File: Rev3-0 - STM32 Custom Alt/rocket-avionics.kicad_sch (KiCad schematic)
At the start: 0 parts

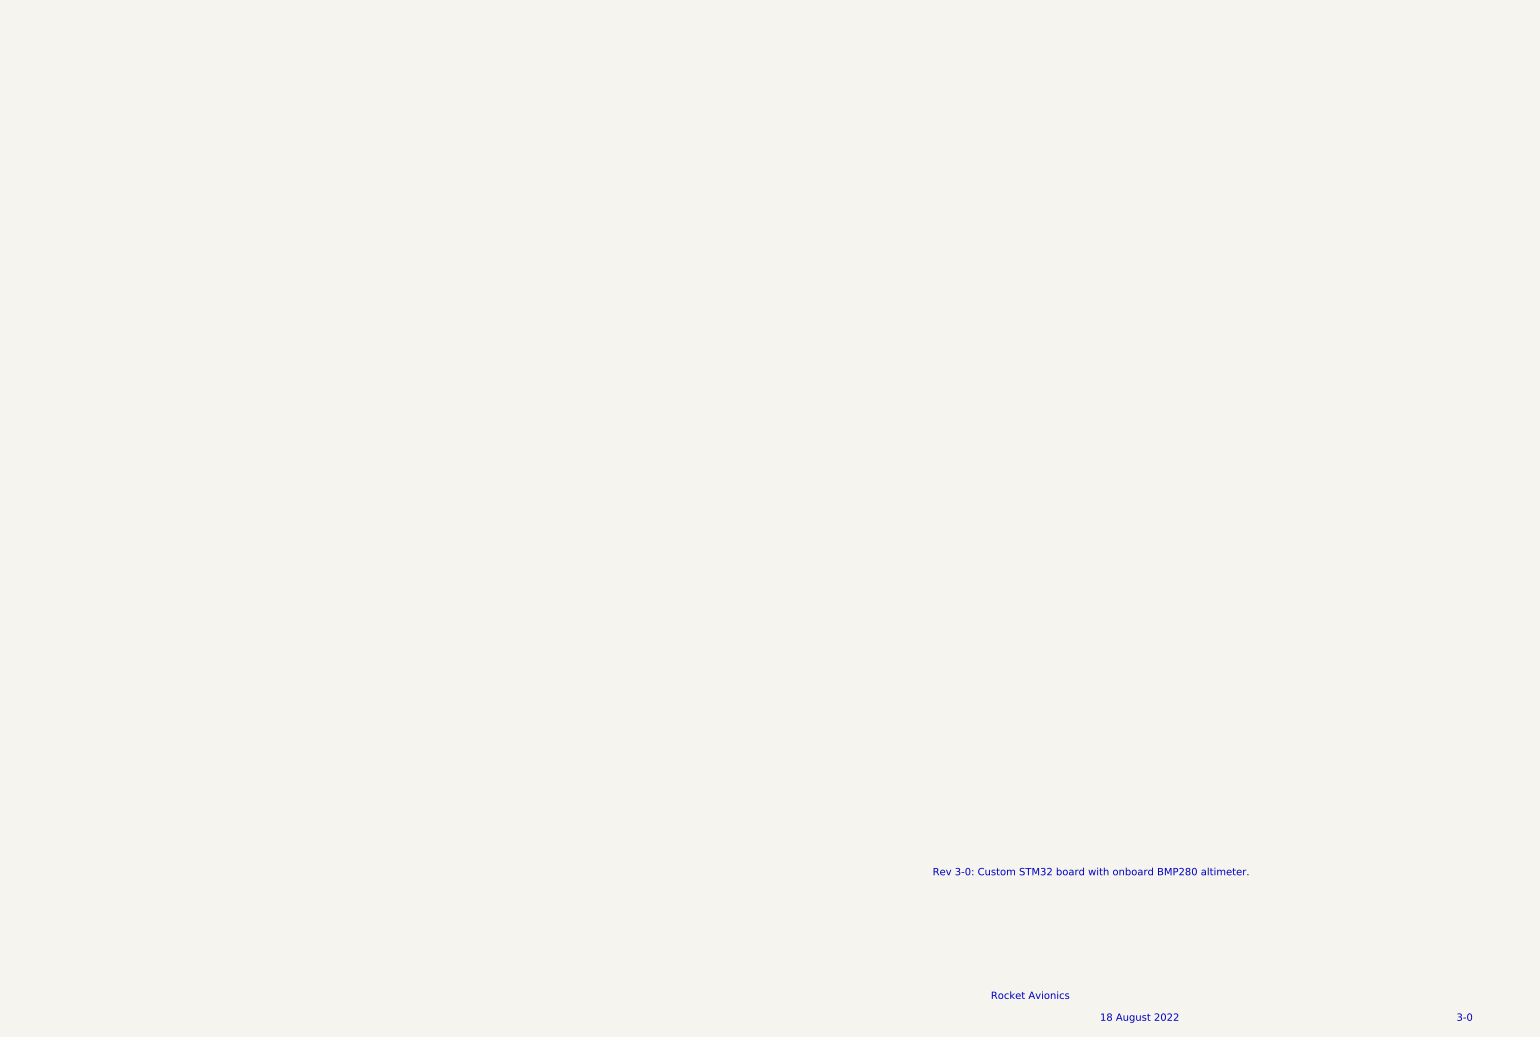
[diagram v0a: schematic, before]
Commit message: Draft schematic for core STM32 circuit.
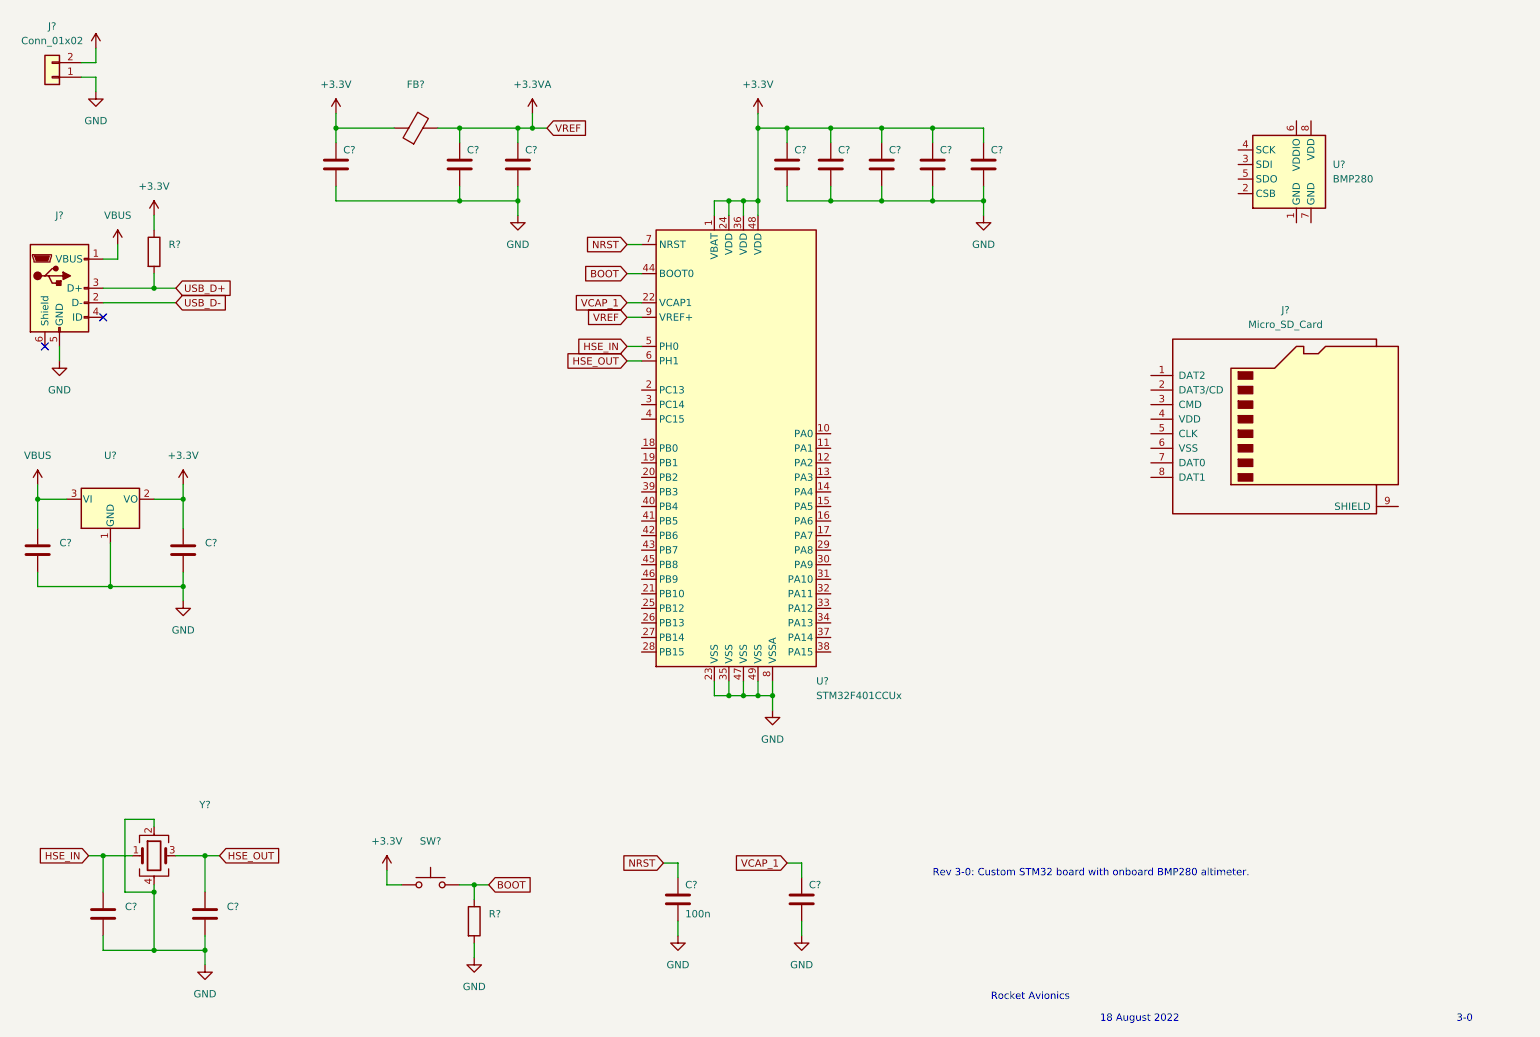
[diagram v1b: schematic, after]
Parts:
- added C? (x13): (no value), symbol Device:C
- added C?: 100n, Capacitor_SMD:C_1206_3216Metric_Pad1.33x1.80mm_HandSolder, symbol Device:C
- added FB?: (no value), symbol Device:FerriteBead
- added J?: (no value), symbol Connector:USB_B_Micro
- added J?: Conn_01x02, symbol Connector_Generic:Conn_01x02
- added J?: Micro_SD_Card, symbol Connector:Micro_SD_Card
- added R? (x2): (no value), symbol Device:R
- added SW?: (no value), symbol Switch:SW_Push
- added U?: BMP280, Package_LGA:Bosch_LGA-8_2x2.5mm_P0.65mm_ClockwisePinNumbering, symbol Sensor_Pressure:BMP280
- added U?: STM32F401CCUx, Package_DFN_QFN:QFN-48-1EP_7x7mm_P0.5mm_EP5.6x5.6mm, symbol MCU_ST_STM32F4:STM32F401CCUx
- added U?: (no value), symbol Regulator_Linear:AMS1117-3.3
- added Y?: (no value), symbol Device:Crystal_GND24
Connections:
- new net +3.3VA: C?.1, C?.1, FB?.2, U?.9 (VREF+)
- new net +3V3: C?.1, C?.1, C?.1, C?.1, C?.1, C?.1, C?.1, FB?.1, R?.1, SW?.1, U?.1 (VBAT), U?.2 (VO), U?.24 (VDD), U?.36 (VDD), U?.48 (VDD)
- new net BOOT: R?.1, SW?.2, U?.44 (BOOT0)
- new net GND: C?.2, C?.2, C?.2, C?.2, C?.2, C?.2, C?.2, C?.2, C?.2, C?.2, C?.2, C?.2, C?.2, C?.2, J?.1 (Pin_1), J?.5 (GND), R?.2, U?.1 (GND), U?.23 (VSS), U?.35 (VSS), U?.47 (VSS), U?.49 (VSS), U?.8 (VSSA), Y?.2, Y?.4
- new net HSE_IN: C?.1, U?.5 (PH0), Y?.1
- new net HSE_OUT: C?.1, U?.6 (PH1), Y?.3
- new net NRST: C?.1, U?.7 (NRST)
- new net USB_D+: J?.3 (D+), R?.2
- new net USB_D-: J?.2 (D-)
- new net VBUS: C?.1, J?.1 (VBUS), J?.2 (Pin_2), U?.3 (VI)
- new net VCAP_1: C?.1, U?.22 (VCAP1)
- no-connect marks 0 -> 2

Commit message: Draft schematic for BMP280 and SD Card.
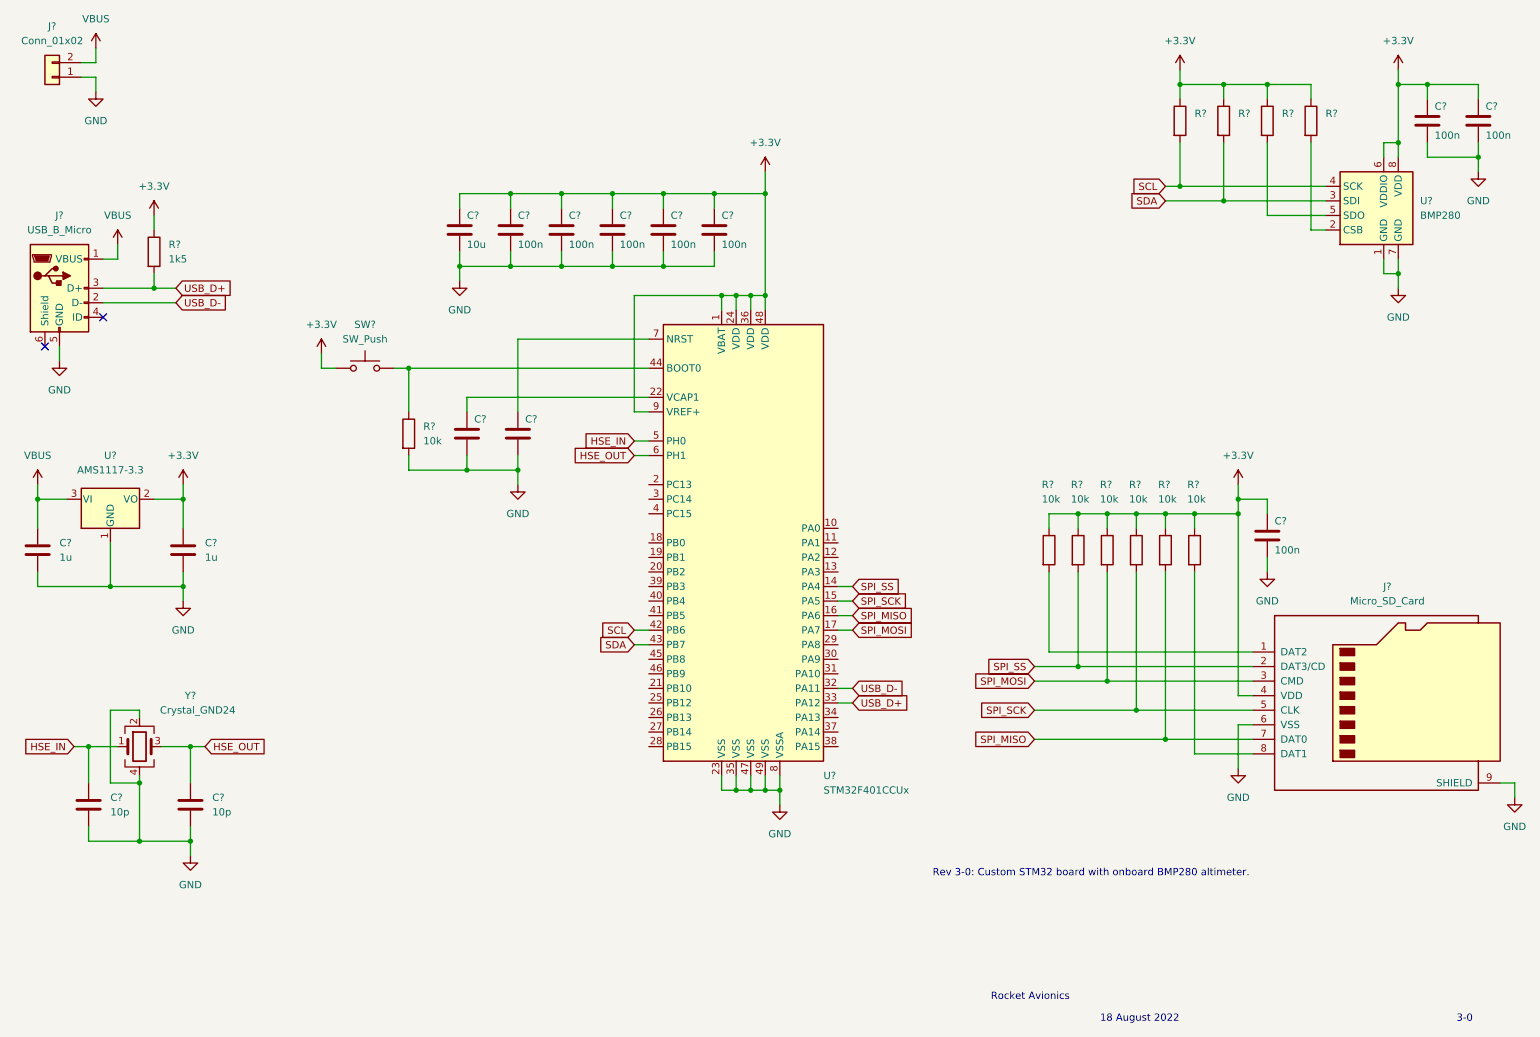
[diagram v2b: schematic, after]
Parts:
- removed C? (x3): (no value), symbol Device:C
- removed FB?: (no value), symbol Device:FerriteBead
- added C? (x4): 100n, Capacitor_SMD:C_1206_3216Metric_Pad1.33x1.80mm_HandSolder, symbol Device:C
- added R? (x4): (no value), symbol Device:R
- added R? (x6): 10k, Resistor_SMD:R_1206_3216Metric_Pad1.30x1.75mm_HandSolder, symbol Device:R
- C? (x4): value (none) -> 100n; footprint (none) -> Capacitor_SMD:C_1206_3216Metric_Pad1.33x1.80mm_HandSolder
- C?: value 100n -> (none); footprint Capacitor_SMD:C_1206_3216Metric_Pad1.33x1.80mm_HandSolder -> (none)
- C? (x2): value (none) -> 10p; footprint (none) -> Capacitor_SMD:C_1206_3216Metric_Pad1.33x1.80mm_HandSolder
- C? (x2): value (none) -> 1u; footprint (none) -> Capacitor_SMD:C_1206_3216Metric_Pad1.33x1.80mm_HandSolder
- C?: value (none) -> 10u; footprint (none) -> Capacitor_SMD:C_1206_3216Metric_Pad1.33x1.80mm_HandSolder
- J?: value (none) -> USB_B_Micro
- R?: value (none) -> 1k5; footprint (none) -> Resistor_SMD:R_1206_3216Metric_Pad1.30x1.75mm_HandSolder
- R?: value (none) -> 10k; footprint (none) -> Resistor_SMD:R_1206_3216Metric_Pad1.30x1.75mm_HandSolder
- SW?: value (none) -> SW_Push
- U?: value (none) -> AMS1117-3.3; footprint (none) -> Package_TO_SOT_SMD:SOT-223-3_TabPin2
- Y?: value (none) -> Crystal_GND24
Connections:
- net +3.3VA is gone; now on net +3V3: U?.9 (VREF+)
- net +3V3: now also J?.4 (VDD), U?.6 (VDDIO), U?.8 (VDD), C?.1, C?.1, C?.1, C?.1, R?.1, R?.1, R?.1, R?.1, R?.1, R?.1, R?.1, R?.1, R?.1, R?.1
- net GND: now also J?.6 (VSS), J?.9 (SHIELD), U?.1 (GND), U?.7 (GND), C?.2, C?.2, C?.2, C?.2
- net USB_D+: now also U?.33 (PA12)
- net USB_D-: now also U?.32 (PA11)
- net at U?.2 (CSB): now also R?.2
- net SDA: now reaches U?.3 (SDI)
- net SDA: now also U?.43 (PB7), R?.2
- net SCL: now reaches U?.4 (SCK)
- net SCL: now also U?.42 (PB6), R?.2
- net at U?.5 (SDO): now also R?.2
- net SPI_SS: now reaches U?.14 (PA4)
- net SPI_SS: now also J?.2 (DAT3/CD), R?.2
- net SPI_SCK: now reaches U?.15 (PA5)
- net SPI_SCK: now also J?.5 (CLK), R?.2
- net SPI_MISO: now reaches U?.16 (PA6)
- net SPI_MISO: now also J?.7 (DAT0), R?.2
- net SPI_MOSI: now reaches U?.17 (PA7)
- net SPI_MOSI: now also J?.3 (CMD), R?.2
- net at J?.1 (DAT2): now also R?.2
- net at J?.8 (DAT1): now also R?.2
- net BOOT: no longer names the net of R?.1, SW?.2, U?.44 (BOOT0)
- net NRST: no longer names the net of C?.1
- net NRST: now also U?.22 (VCAP1); no longer U?.7 (NRST)
- net VCAP_1: no longer names the net of C?.1
- net VCAP_1: now also U?.7 (NRST); no longer U?.22 (VCAP1)
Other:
- moved on the sheet: C?, J?, R?, SW?, U?, Y?
